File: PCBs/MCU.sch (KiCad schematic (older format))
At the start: 19 parts, among them J10 SPK, J7 Conn_01x10, U1 24LC01, U6 Arduino_Nano

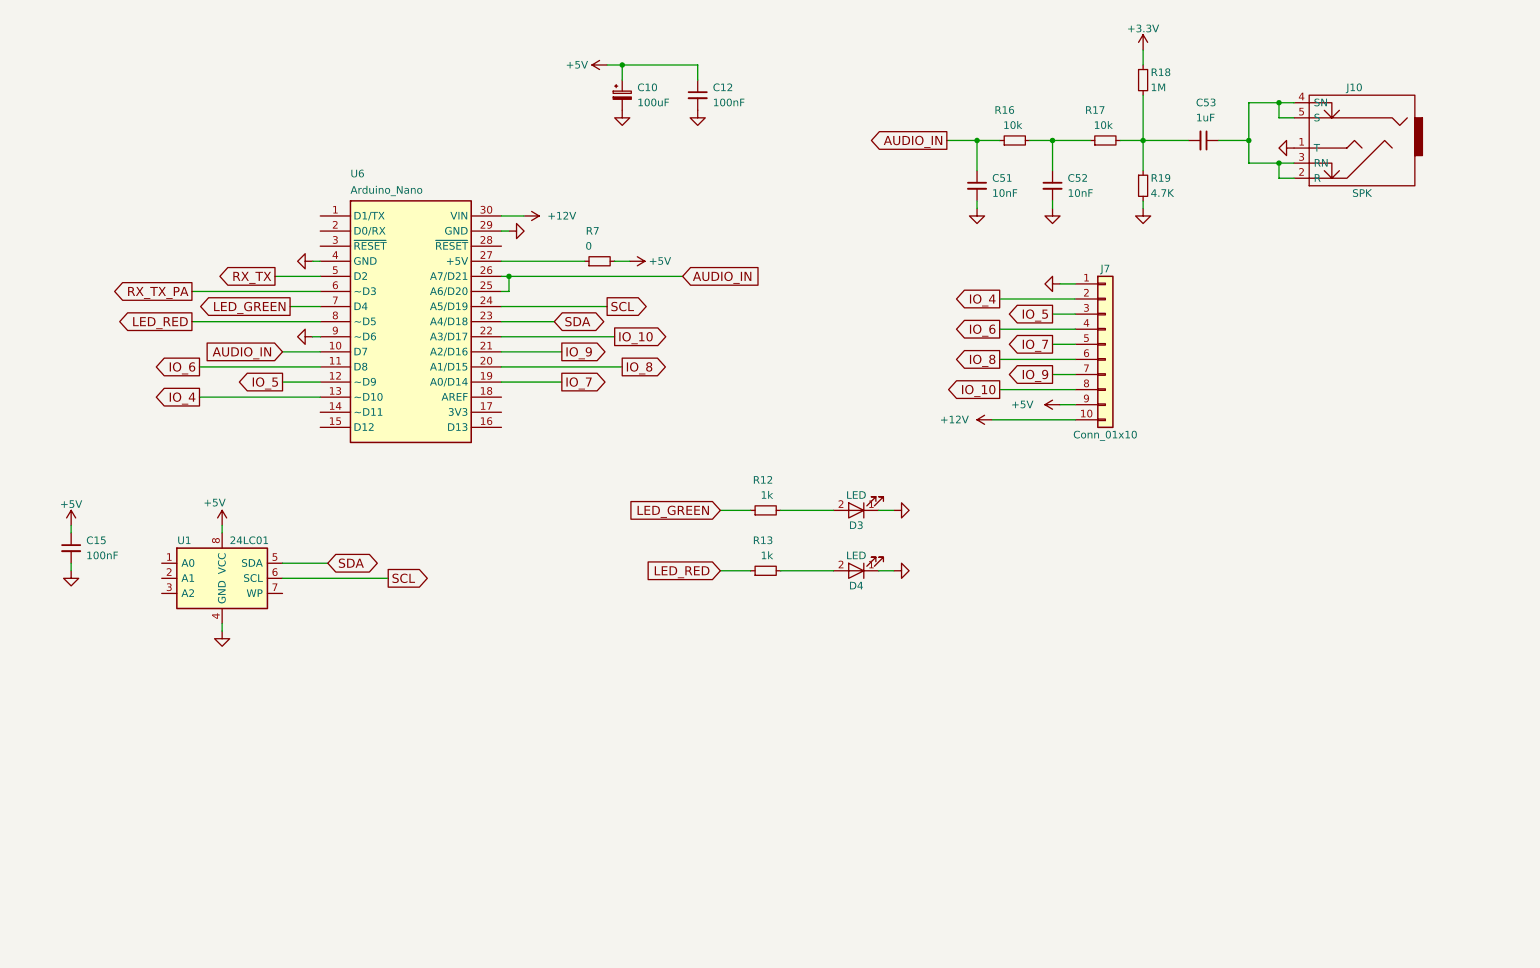
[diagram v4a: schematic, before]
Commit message: migrate to attiny1614
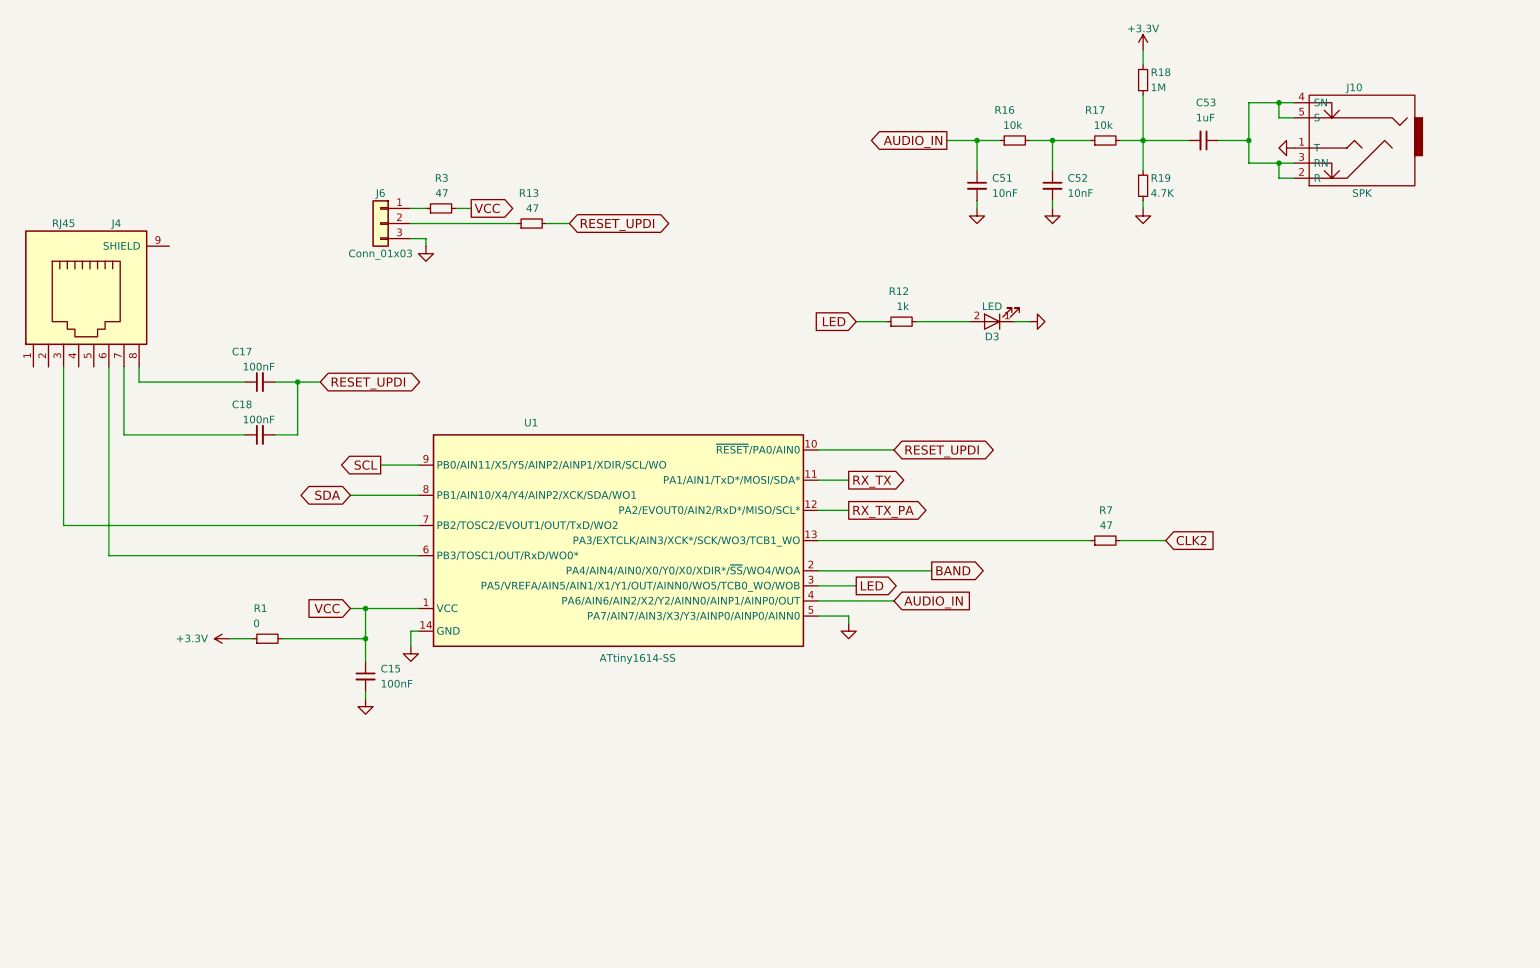
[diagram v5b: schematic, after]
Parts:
- removed C10: 100uF, Capacitors_THT:CP_Radial_D6.3mm_P2.50mm, symbol CP_Small
- removed C12: 100nF, Capacitors_SMD:C_0603_HandSoldering, symbol C_Small
- removed D4: LED, LEDs:LED_0603_HandSoldering, symbol LED
- removed J7: Conn_01x10, Pin_Headers:Pin_Header_Straight_1x10_Pitch2.54mm, symbol Conn_01x10
- removed U1: 24LC01, Housings_SOIC:SOIC-8_3.9x4.9mm_Pitch1.27mm, symbol 24LC01
- removed U6: Arduino_Nano, Arduino:Arduino_Nano, symbol Arduino_Nano
- added C17, C18: 100nF, Capacitors_SMD:C_0603_HandSoldering, symbol C_Small
- added J4: RJ45, Connectors:RJ45_8, symbol RJ45
- added J6: Conn_01x03, Pin_Headers:Pin_Header_Straight_1x03_Pitch2.54mm, symbol Conn_01x03
- added R1: 0, Resistors_SMD:R_0603_HandSoldering, symbol R_Small
- added R3: 47, Resistors_SMD:R_0603_HandSoldering, symbol R_Small
- added U1: ATtiny1614-SS, Housings_SOIC:SOIC-14_3.9x8.7mm_Pitch1.27mm, symbol ATtiny1604-SS
- R13: value 1k -> 47
- R7: value 0 -> 47
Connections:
- net +3V3: now also R1.1
- net AUDIO_IN: now also U1.4 (PA6/AIN6/AIN2/X2/Y2/AINN0/AINP1/AINP0/OUT)
- net GND: now also J6.3 (Pin_3), U1.14 (GND), U1.5 (PA7/AIN7/AIN3/X3/Y3/AINP0/AINP0/AINN0)
- net RX_TX: now also U1.11 (PA1/AIN1/TxD*/MOSI/SDA*)
- net RX_TX_PA: now also U1.12 (PA2/EVOUT0/AIN2/RxD*/MISO/SCL*)
- net SCL: now also U1.9 (PB0/AIN11/X5/Y5/AINP2/AINP1/XDIR/SCL/WO)
- net SDA: now also U1.8 (PB1/AIN10/X4/Y4/AINP2/XCK/SDA/WO1)
- net RESET_UPDI: now reaches R13.2
- net RESET_UPDI: now also C17.2, C18.2, U1.10 (~RESET~/PA0/AIN0)
- net at R7.1: now also U1.13 (PA3/EXTCLK/AIN3/XCK*/SCK/WO3/TCB1_WO)
- net +5V renamed CLK2
- net CLK2: no longer C15.1
- net LED_GREEN renamed LED
- net LED: now also U1.3 (PA5/VREFA/AIN5/AIN1/X1/Y1/OUT/AINN0/WO5/TCB0_WO/WOB)
- net LED_RED: no longer names the net of R13.1
- net LED_RED: now also J6.2 (Pin_2)
- new net: J4.6, U1.6 (PB3/TOSC1/OUT/RxD/WO0*)
- new net: J4.3, U1.7 (PB2/TOSC2/EVOUT1/OUT/TxD/WO2)
- new net: C18.1, J4.7
- new net: C17.1, J4.8
- new net: J6.1 (Pin_1), R3.1
- new net BAND: U1.2 (PA4/AIN4/AIN0/X0/Y0/X0/XDIR*/~SS~/WO4/WOA)
- new net VCC: C15.1, R1.2, R3.2, U1.1 (VCC)
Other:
- moved on the sheet: C15, D3, R12
